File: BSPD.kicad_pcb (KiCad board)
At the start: 2 copper layers, 96.5 x 71.1 mm, 63 parts, among them J1 Conn_01x14, K1 MCCMA51-S-DC12V-C, Q1 IRLZ44Z, U1 4011, U10 LM317_SOT-223, U11 4012, U12 74LS573, U13 4040, U14 4040, U15 4040, U17 MAX6895, U2 4011, U3 4011, U4 4011, U5 4011, U6 4011, U7 4011, U9 TLC3704, X1 ASZKDV-32.768KHz

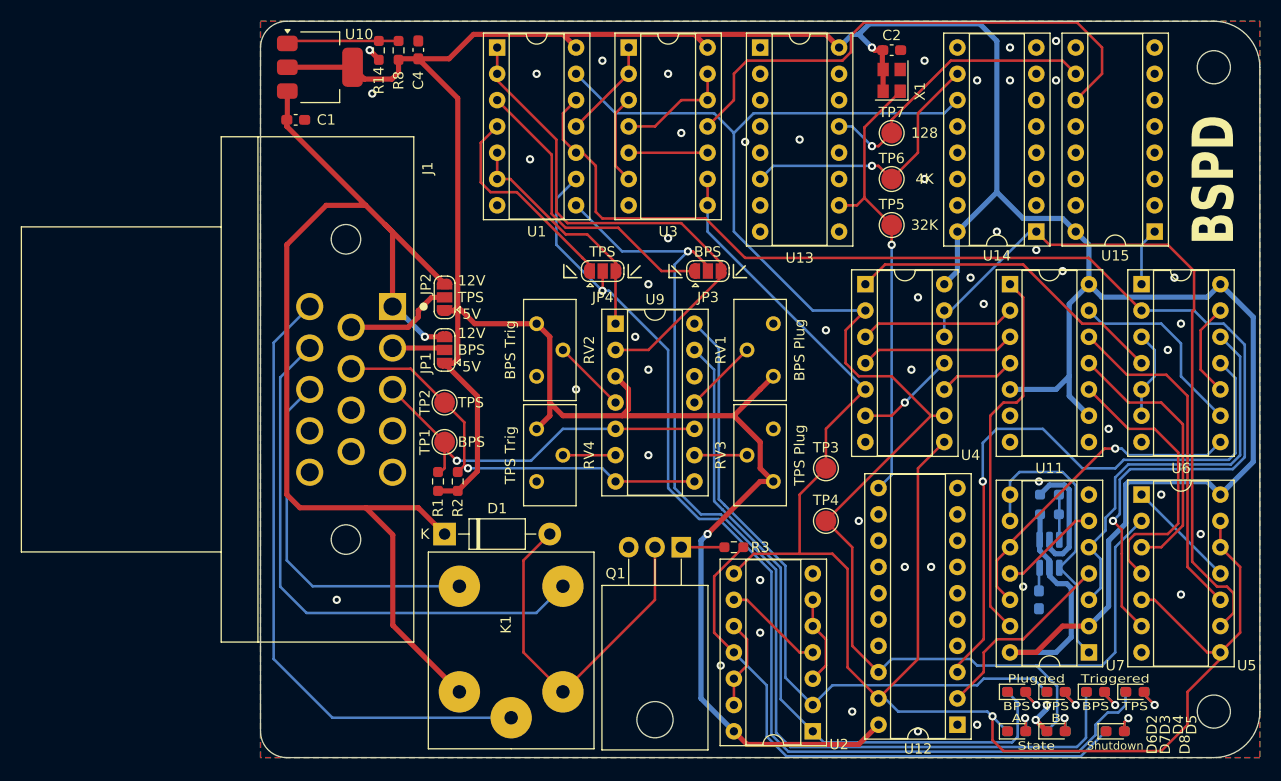
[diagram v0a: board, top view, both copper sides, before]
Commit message: Misc improvements and changes.
- Updated some silkscreen
- Added 2 more mounting holes, changed them to pads
- Updated FBR Logo
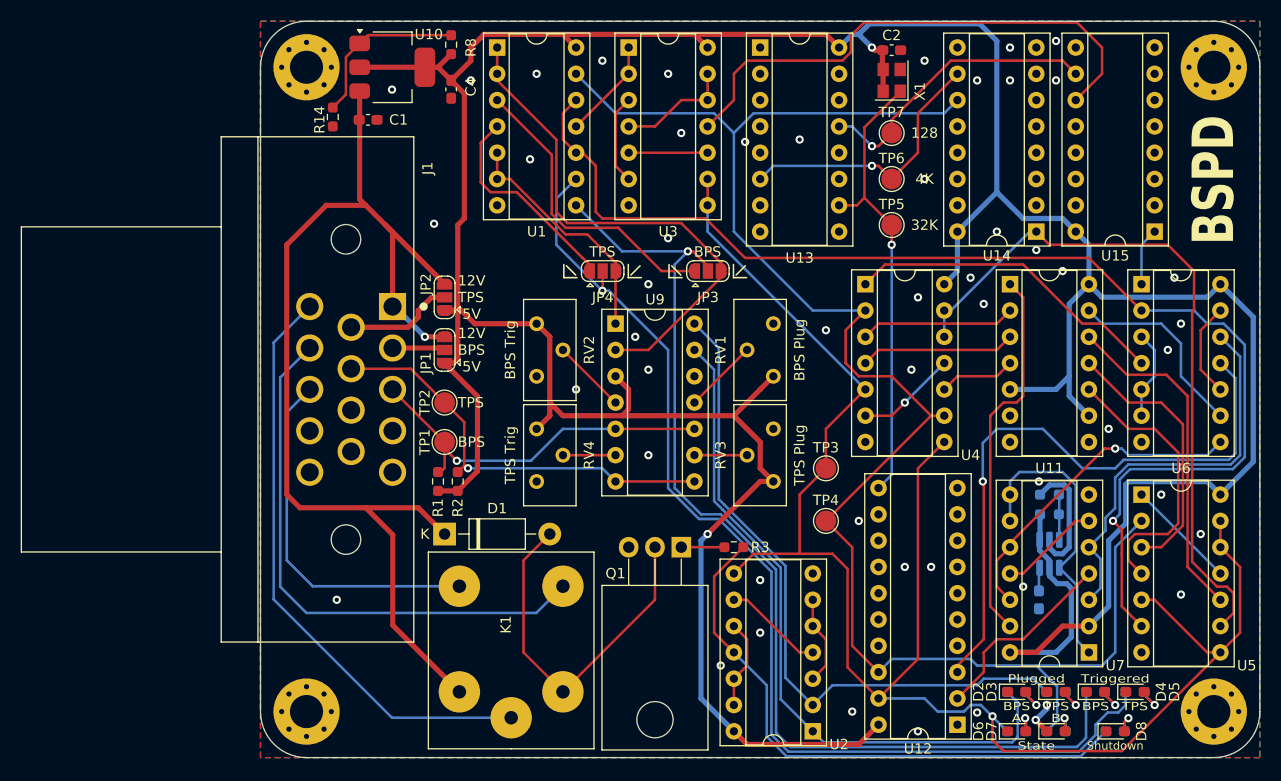
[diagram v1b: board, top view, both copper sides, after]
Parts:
- removed MNT1, MNT2: MountingHole_3.2mm_M3, MountingHole:MountingHole_3.2mm_M3
- added H1: MountingHole_Pad, MountingHole:MountingHole_3.2mm_M3_Pad_Via, F.Cu at (144.1, 27.3)
- added H2: MountingHole_Pad, MountingHole:MountingHole_3.2mm_M3_Pad_Via, F.Cu at (144.1, 89.5)
- added H3: MountingHole_Pad, MountingHole:MountingHole_3.2mm_M3_Pad_Via, F.Cu at (56.5, 89.5)
- added H4: MountingHole_Pad, MountingHole:MountingHole_3.2mm_M3_Pad_Via, F.Cu at (56.5, 27.3)
- G***: footprint BSPD_footprints:FBR_Logo_.9in -> FBR_Footprints:FBR_Logo_.9in
- moved G*** 12.0 mm to (148.8, 30.6)
- moved R14 7.82 mm to (59.1, 32.1)
- moved C1 6.99 mm to (62.5, 32.4)
- moved U10 6.98 mm to (64.8, 27.3)
- moved R8 5.11 mm to (70.5, 25.1)
- moved C4 4.96 mm to (70.5, 29.4), turned to -90 degrees
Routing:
- net +5V: track 385.7 -> 377.8 mm
- net Net-(U10-ADJ): track 10.8 -> 16.4 mm
- net /ShutdownC: track 60.8 -> 57.4 mm
- net +12V: track 111.1 -> 108.1 mm
- net /SM_Ok: track 167.3 -> 165.6 mm
- net GND: track 16.9 -> 15.6 mm, vias 51 -> 52
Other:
- outline, holes or cut-outs redrawn
- board text added: "Designed by Oliver Gaskell, Jan 2025"
- board text removed: "Designed by Oliver Gaskell, Dec 2024"

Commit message: Small changes, post design review
- Moving tracks away from PCB edge
- Added jumper, can be used to short shutdown
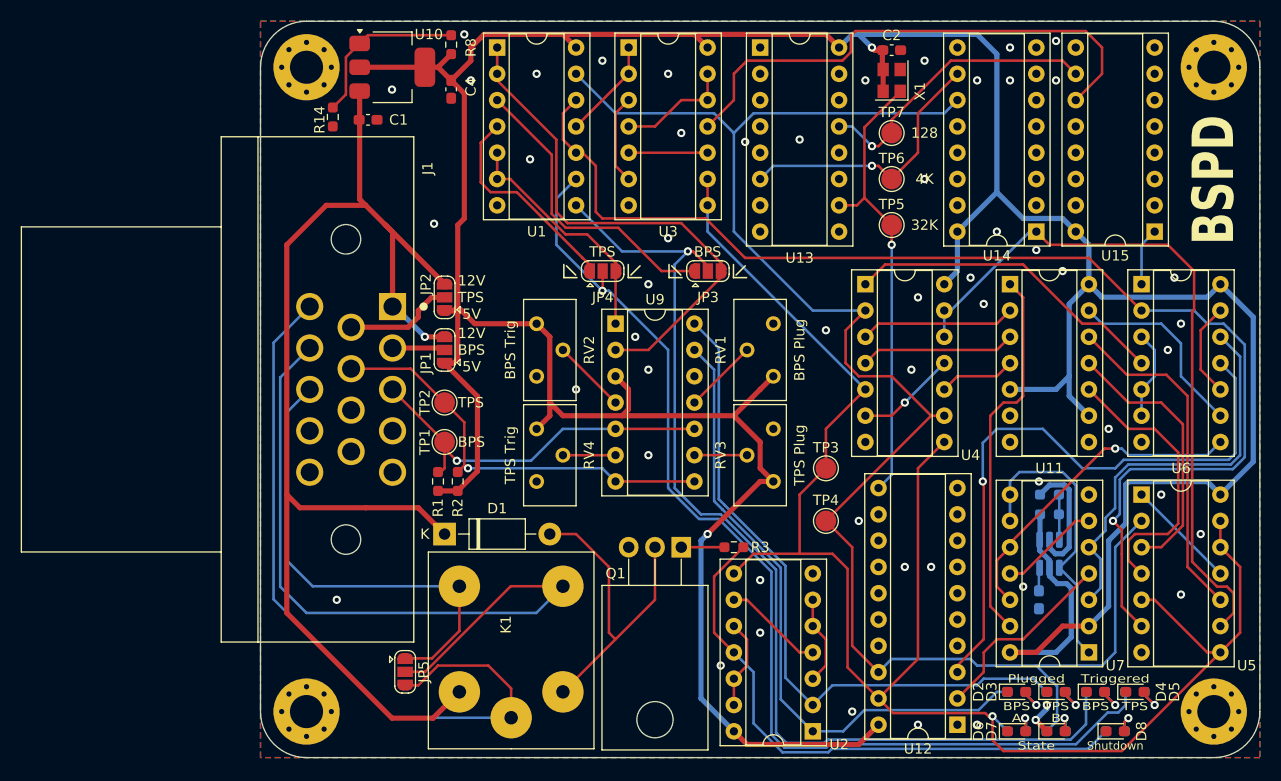
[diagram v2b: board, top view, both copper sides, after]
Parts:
- added JP5: SolderJumper_3_Open, Jumper:SolderJumper-3_P1.3mm_Open_RoundedPad1.0x1.5mm, F.Cu at (66.0, 85.7)
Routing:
- net /ShutdownNC: track 53.7 -> 72.3 mm
- net /ShutdownC: track 57.4 -> 72.2 mm
- net +12V: track 108.1 -> 120.0 mm
- net /ShutdownNO: track 35.1 -> 45.8 mm
- net /BPS_Plugged: track 66.8 -> 61.9 mm
- net Net-(D1-A): track 35.5 -> 31.9 mm
- net +5V: track 377.8 -> 376.2 mm
- net /BPS_Trig: track 103.1 -> 102.0 mm
- net /TPS_Trig: track 105.1 -> 104.2 mm
- net /State Machine/Timers/Reset_Counting: track 51.8 -> 51.1 mm
- net /SM_Ok: track 165.6 -> 165.1 mm
- net GND: vias 52 -> 54
